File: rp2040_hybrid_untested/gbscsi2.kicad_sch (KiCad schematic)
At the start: 150 parts, among them J1 USB_DATA, J2 TF003, J3 Conn_01x02, J4 Conn_01x04, J5 SCSI_50-2P_2mm, J6 SCSI_50P_2.54mm, J7 Conn_01x04, Q1 AO3401A, Q10 AO3401A, Q11 AO3401A, Q12 AO3401A, Q13 AO3401A, Q14 AO3401A, Q15 AO3401A, Q16 AO3401A, Q17 AO3401A, Q18 AO3401A, Q2 AO3401A, Q3 AO3401A, Q4 AO3401A, Q5 AO3401A, Q6 AO3401A, Q7 AO3401A, Q8 AO3401A, Q9 AO3401A, SW1 SW_DIP_x04, U2 W25Q128JVS, U3 RP2040, U4 74AHCT1G125, U7 AZ1117-2.85, U8 AP62250WU, U9 USB TVS, Y1 12MHz

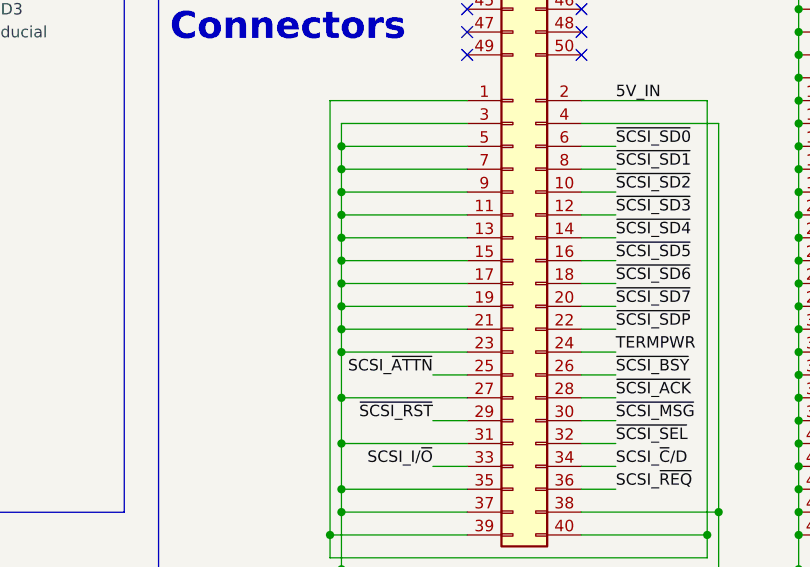
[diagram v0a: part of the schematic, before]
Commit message: Changed diodes in BoM, minor corrections to PCB, documentation
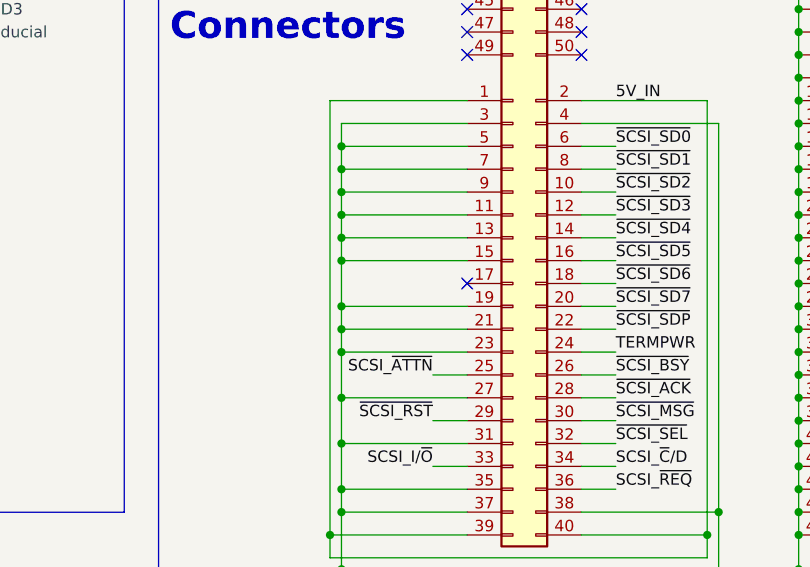
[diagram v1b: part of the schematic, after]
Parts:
- D? (x4): LCSC C8598 -> C82544
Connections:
- net GND: no longer J5.17 (Pin_17)
- no-connect marks 13 -> 14
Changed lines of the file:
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@@
   (junction (at 481.33 24.13) (diameter 0) (color 0 0 0 0)
   )
+  (junction (at 430.53 57.15) (diameter 0) (color 0 0 0 0)
+  )
   (junction (at 288.29 27.94) (diameter 0) (color 0 0 0 0)
   )
@@
   (junction (at 181.61 142.24) (diameter 0) (color 0 0 0 0)
   )
-  (junction (at 430.53 57.15) (diameter 0) (color 0 0 0 0)
-  )
   (junction (at 430.53 44.45) (diameter 0) (color 0 0 0 0)
   )
@@
   (junction (at 439.42 158.75) (diameter 0) (color 0 0 0 0)
   )
-  (junction (at 430.53 52.07) (diameter 0) (color 0 0 0 0)
-  )
   (junction (at 481.33 77.47) (diameter 0) (color 0 0 0 0)
   )
   (no_connect (at 105.41 104.14))
   (no_connect (at 105.41 101.6))
+  (no_connect (at 444.5 52.07))
   (no_connect (at 55.88 242.57))
   (no_connect (at 457.2 21.59))
@@
     (stroke (width 0) (type default))
   )
+  (wire (pts (xy 430.53 57.15) (xy 430.53 59.69))
+    (stroke (width 0) (type default))
+  )
   (wire (pts (xy 430.53 69.85) (xy 444.5 69.85))
     (stroke (width 0) (type default))
@@
     (stroke (width 0) (type default))
   )
+  (wire (pts (xy 430.53 57.15) (xy 444.5 57.15))
+    (stroke (width 0) (type default))
+  )
   (wire (pts (xy 66.04 167.64) (xy 58.42 167.64))
     (stroke (width 0) (type default))
@@
     (stroke (width 0) (type default))
   )
-  (wire (pts (xy 430.53 57.15) (xy 444.5 57.15))
-    (stroke (width 0) (type default))
-  )
   (wire (pts (xy 241.3 200.66) (xy 241.3 198.12))
     (stroke (width 0) (type default))
@@
     (stroke (width 0) (type default))
   )
-  (wire (pts (xy 430.53 52.07) (xy 444.5 52.07))
-    (stroke (width 0) (type default))
-  )
   (wire (pts (xy 303.53 200.66) (xy 303.53 198.12))
     (stroke (width 0) (type default))
@@
     (stroke (width 0) (type default))
   )
-  (wire (pts (xy 430.53 49.53) (xy 430.53 52.07))
-    (stroke (width 0) (type default))
-  )
   (wire (pts (xy 461.01 64.77) (xy 457.2 64.77))
     (stroke (width 0) (type default))
@@
     (stroke (width 0) (type default))
   )
-  (wire (pts (xy 430.53 52.07) (xy 430.53 54.61))
+  (wire (pts (xy 430.53 49.53) (xy 430.53 54.61))
     (stroke (width 0) (type default))
   )
-  (wire (pts (xy 430.53 57.15) (xy 430.53 59.69))
+  (wire (pts (xy 430.53 54.61) (xy 430.53 57.15))
     (stroke (width 0) (type default))
   )
@@
     (stroke (width 0) (type default))
   )
-  (wire (pts (xy 430.53 54.61) (xy 430.53 57.15))
-    (stroke (width 0) (type default))
-  )
   (wire (pts (xy 472.44 116.84) (xy 482.6 116.84))
     (stroke (width 0) (type default))
@@
       (effects (font (size 1.27 1.27)))
     )
-    (property "LCSC" "C8598" (at 281.94 27.94 0)
+    (property "LCSC" "C82544" (at 281.94 27.94 0)
       (effects (font (size 1.27 1.27)) hide)
     )
@@
       (effects (font (size 1.27 1.27)))
     )
-    (property "LCSC" "C8598" (at 274.32 35.56 0)
+    (property "LCSC" "C82544" (at 274.32 35.56 0)
       (effects (font (size 1.27 1.27)) hide)
     )
@@
       (effects (font (size 1.27 1.27)))
     )
-    (property "LCSC" "C8598" (at 281.94 57.15 0)
+    (property "LCSC" "C82544" (at 281.94 57.15 0)
       (effects (font (size 1.27 1.27)) hide)
     )
@@
       (effects (font (size 1.27 1.27)))
     )
-    (property "LCSC" "C8598" (at 281.94 66.04 0)
+    (property "LCSC" "C82544" (at 281.94 66.04 0)
       (effects (font (size 1.27 1.27)) hide)
     )

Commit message: BoM fixes for discrete variants, interactive BoMs added to each major type, mfg files for 2350
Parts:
- R1, R5: LCSC C21190 -> C11702
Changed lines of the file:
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@@
       (effects (font (size 1.27 1.27)) hide)
     )
-    (property "LCSC" "C21190" (at 46.99 167.64 0)
+    (property "LCSC" "C11702" (at 46.99 167.64 0)
       (effects (font (size 1.27 1.27)) hide)
     )
@@
       (effects (font (size 1.27 1.27)) hide)
     )
-    (property "LCSC" "C21190" (at 193.04 52.07 0)
+    (property "LCSC" "C11702" (at 193.04 52.07 0)
       (effects (font (size 1.27 1.27)) hide)
     )

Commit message: Re-sorting things around
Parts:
- removed C19: 4.7nF, Capacitor_SMD:C_0402_1005Metric, symbol Device:C_Small
- removed R?: 1M, Resistor_SMD:R_0402_1005Metric, symbol zuluscsi-rescue:R
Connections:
- net GND: now also J1.S1 (SHIELD)
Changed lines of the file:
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@@
   (junction (at 472.44 182.88) (diameter 0) (color 0 0 0 0)
   )
-  (junction (at 55.88 257.81) (diameter 0) (color 0 0 0 0)
-  )
   (junction (at 481.33 69.85) (diameter 0) (color 0 0 0 0)
   )
@@
   (junction (at 55.88 215.9) (diameter 0) (color 0 0 0 0)
   )
-  (junction (at 66.04 265.43) (diameter 0.9144) (color 0 0 0 0)
-  )
   (junction (at 181.61 142.24) (diameter 0) (color 0 0 0 0)
   )
@@
   (junction (at 340.36 156.21) (diameter 0) (color 0 0 0 0)
   )
-  (junction (at 59.69 265.43) (diameter 0) (color 0 0 0 0)
+  (junction (at 66.04 257.81) (diameter 0) (color 0 0 0 0)
   )
   (junction (at 127 91.44) (diameter 0) (color 0 0 0 0)
@@
     (stroke (width 0) (type default))
   )
-  (wire (pts (xy 55.88 265.43) (xy 59.69 265.43))
-    (stroke (width 0) (type solid))
-  )
   (wire (pts (xy 158.75 176.53) (xy 153.67 176.53))
     (stroke (width 0) (type default))
@@
     (stroke (width 0) (type default))
   )
-  (wire (pts (xy 66.04 254) (xy 66.04 265.43))
-    (stroke (width 0) (type solid))
-  )
   (wire (pts (xy 175.26 201.93) (xy 139.7 201.93))
     (stroke (width 0) (type default))
@@
     (stroke (width 0) (type default))
   )
-  (wire (pts (xy 59.69 265.43) (xy 66.04 265.43))
-    (stroke (width 0) (type solid))
-  )
   (wire (pts (xy 168.91 186.69) (xy 168.91 204.47))
     (stroke (width 0) (type default))
@@
     (stroke (width 0) (type default))
   )
-  (wire (pts (xy 66.04 265.43) (xy 66.04 266.7))
+  (wire (pts (xy 66.04 254) (xy 66.04 257.81))
     (stroke (width 0) (type solid))
   )
@@
     (stroke (width 0) (type default))
   )
-  (wire (pts (xy 59.69 257.81) (xy 59.69 259.08))
-    (stroke (width 0) (type solid))
-  )
   (wire (pts (xy 143.51 123.19) (xy 143.51 124.46))
     (stroke (width 0) (type default))
@@
     (stroke (width 0) (type default))
   )
-  (wire (pts (xy 59.69 264.16) (xy 59.69 265.43))
-    (stroke (width 0) (type solid))
-  )
   (wire (pts (xy 106.68 119.38) (xy 106.68 124.46))
     (stroke (width 0) (type default))
   )
-  (wire (pts (xy 55.88 257.81) (xy 59.69 257.81))
+  (wire (pts (xy 55.88 257.81) (xy 66.04 257.81))
     (stroke (width 0) (type solid))
   )
@@
     (stroke (width 0) (type default))
   )
+  (wire (pts (xy 66.04 257.81) (xy 66.04 266.7))
+    (stroke (width 0) (type solid))
+  )
   (wire (pts (xy 274.32 27.94) (xy 274.32 31.75))
     (stroke (width 0) (type default))
@@
     )
   )
-  (symbol (lib_id "zuluscsi-rescue:R") (at 55.88 261.62 0) (mirror y) (unit 1)
-    (in_bom yes) (on_board yes) (dnp no)
-    (property "Reference" "R?" (at 53.34 261.62 90)
-      (effects (font (size 1.27 1.27)))
-    )
-    (property "Value" "1M" (at 55.88 261.62 90)
-      (effects (font (size 1.27 1.27)))
-    )
-    (property "Footprint" "Resistor_SMD:R_0402_1005Metric" (at 57.658 261.62 90)
-      (effects (font (size 1.27 1.27)) hide)
-    )
-    (property "Datasheet" "" (at 55.88 261.62 0)
-      (effects (font (size 1.27 1.27)))
-    )
-    (property "LCSC" "C26083" (at 55.88 261.62 0)
-      (effects (font (size 1.27 1.27)) hide)
-    )
-    (pin "1")
-    (pin "2")
-    (instances
-      (project "ZuluSCSI-Pico-OSHW"
-        (path "/0a1a4d88-972a-46ce-b25e-6cb796bd41f7/00000000-0000-0000-0000-000055ff7cc4"
-          (reference "R?") (unit 1)
-        )
-      )
-      (project "cpu"
-        (path "/45b7fe01-a2fa-40c2-a3a2-4a9ae7c34dba"
-          (reference "R?") (unit 1)
-        )
-      )
-      (project "gbscsi2"
-        (path "/81c2a5db-c508-405c-87d7-d49be9ddd5e4"
-          (reference "R15") (unit 1)
-        )
-      )
-    )
-  )
   (symbol (lib_id "Device:C") (at 224.79 38.1 0) (unit 1)
     (in_bom yes) (on_board yes) (dnp no)
@@
         )
       )
-    )
-  )
-  (symbol (lib_id "Device:C_Small") (at 59.69 261.62 0) (mirror y) (unit 1)
-    (in_bom yes) (on_board yes) (dnp no)
-    (property "Reference" "C19" (at 63.5 259.08 0)
-      (effects (font (size 1.27 1.27)) (justify left))
-    )
-    (property "Value" "4.7nF" (at 66.04 264.16 0)
-      (effects (font (size 1.27 1.27)) (justify left))
-    )
-    (property "Footprint" "Capacitor_SMD:C_0402_1005Metric" (at 59.69 261.62 0)
-      (effects (font (size 1.27 1.27)) hide)
-    )
-    (property "Datasheet" "~" (at 59.69 261.62 0)
-      (effects (font (size 1.27 1.27)) hide)
-    )
-    (property "LCSC" "C346200" (at 59.69 261.62 0)
-      (effects (font (size 1.27 1.27)) hide)
-    )
-    (pin "1")
-    (pin "2")
-    (instances
-      (project "gbscsi2"
-        (path "/81c2a5db-c508-405c-87d7-d49be9ddd5e4"
-          (reference "C19") (unit 1)
-        )
-      )
-      (project "poe_hat_v1.4.2"
-        (path "/84fe1d92-0d61-4eda-acb4-e2fc63573041"
-          (reference "C8") (unit 1)
-        )
-      )

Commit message: Cleaning up, updating docs
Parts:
- C1: value 100nF -> 10uF; LCSC C14663 -> C96446
- C? (x17): symbol zuluscsi-rescue:C_Small -> Device:C_Small
- D? (x4): symbol zuluscsi-rescue:D_Schottky -> Device:D_Schottky
- R? (x27): symbol zuluscsi-rescue:R -> Device:R
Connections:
- net +3V3: no longer C1.1, C?.1, C?.1, C?.1, C?.1, C?.1, C?.1, C?.1, C?.1, J2.4 (VDD), J7.1 (Pin_1), L2.2, R?.1, R?.1, R?.1, R?.1, R?.1, R?.1, R?.1, R?.2, R?.2, R?.2, R?.2, R?.2, R?.2, U4.5 (VCC), U?.14 (VCC), U?.14 (VCC), U?.20 (VCC), U?.20 (VCC)
- new net +3.3V: C1.1, C?.1, C?.1, C?.1, C?.1, C?.1, C?.1, C?.1, C?.1, J2.4 (VDD), J7.1 (Pin_1), L2.2, R?.1, R?.1, R?.1, R?.1, R?.1, R?.1, R?.1, R?.2, R?.2, R?.2, R?.2, R?.2, R?.2, U4.5 (VCC), U?.14 (VCC), U?.14 (VCC), U?.20 (VCC), U?.20 (VCC)
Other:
- moved on the sheet: C?
